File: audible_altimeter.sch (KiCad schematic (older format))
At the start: 12 parts, among them IC1 BUQ2-ATXMEGA128A4U-A, U1 MPL3115A2, U2 TAG-CONNECT-ATMEL-PDI-CONNECT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, U3 MICRO-SD-CONN, U4 MPU-9250, U5 MCP7940M, U6 MCP73831-SOT-23-5, U7 NCP4681-SC-70, U8 CSS-0575A-SMT, U9 LS013B4DN04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

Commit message: Component assignements
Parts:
- removed CON?: BUQ2-USB-MICRO-B, BUQ2-USB-MICRO-B-RIGHT-ANGLE-SM, symbol BUQ2-USB-MICRO-B
- added CON1: BUQ2-USB-MICRO-B, buq2:USB-MICRO-B-FCI, symbol BUQ2-USB-MICRO-B
- U1: footprint (none) -> buq2:8-TLGA
- U3: footprint (none) -> buq2:MICRO-SD-CONN-AMPHENOL-PUSH-PUSH
- U5: footprint (none) -> buq2:8-TDFN
- U6: footprint (none) -> buq2:SOT-23-5
- U7: footprint (none) -> buq2:SOT-353
- U8: footprint (none) -> buq2:BUZZER-CUI-5MM
- U9: footprint (none) -> buq2:FPC-CONN-10-FCI
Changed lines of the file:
@@
 F 0 "U1" H 3850 5950 60  0000 C CNN
 F 1 "MPL3115A2" H 3850 5150 60  0000 C CNN
-F 2 "" H 3850 5550 60  0001 C CNN
+F 2 "buq2:8-TLGA" H 3850 5550 60  0001 C CNN
 F 3 "" H 3850 5550 60  0000 C CNN
 	1    3850 5550
@@
 F 0 "U5" H 6300 4500 60  0000 C CNN
 F 1 "MCP7940M" H 6300 5500 60  0000 C CNN
-F 2 "" H 6350 4850 60  0001 C CNN
+F 2 "buq2:8-TDFN" H 6350 4850 60  0001 C CNN
 F 3 "" H 6350 4850 60  0000 C CNN
 	1    6350 4850
@@
 F 0 "U9" H 10100 3550 60  0000 C CNN
 F 1 "LS013B4DN04" H 10050 5500 60  0000 C CNN
-F 2 "" H 9750 4700 60  0001 C CNN
+F 2 "buq2:FPC-CONN-10-FCI" H 9750 4700 60  0001 C CNN
 F 3 "" H 9750 4700 60  0000 C CNN
 	1    9750 4700
@@
 F 0 "U8" H 9650 3000 60  0000 C CNN
 F 1 "CSS-0575A-SMT" H 9750 3950 60  0000 C CNN
-F 2 "" H 9400 3050 60  0001 C CNN
+F 2 "buq2:BUZZER-CUI-5MM" H 9400 3050 60  0001 C CNN
 F 3 "" H 9400 3050 60  0000 C CNN
 	1    9400 3050
@@
 F 0 "U6" H 8100 6200 60  0000 C CNN
 F 1 "MCP73831-SOT-23-5" H 8100 7100 60  0000 C CNN
-F 2 "" H 8100 6200 60  0001 C CNN
+F 2 "buq2:SOT-23-5" H 8100 6200 60  0001 C CNN
 F 3 "" H 8100 6200 60  0000 C CNN
 	1    8100 6200
@@
 F 0 "U3" H 5850 6300 60  0000 C CNN
 F 1 "MICRO-SD-CONN" H 5850 7850 60  0000 C CNN
-F 2 "" H 5850 6950 60  0001 C CNN
+F 2 "buq2:MICRO-SD-CONN-AMPHENOL-PUSH-PUSH" H 5850 6950 60  0001 C CNN
 F 3 "" H 5850 6950 60  0000 C CNN
 	1    5850 6950
@@
 F 0 "U7" H 8750 950 60  0000 C CNN
 F 1 "NCP4681-SC-70" H 8800 1750 60  0000 C CNN
-F 2 "" H 8750 850 60  0001 C CNN
+F 2 "buq2:SOT-353" H 8750 850 60  0001 C CNN
 F 3 "" H 8750 850 60  0000 C CNN
 	1    8750 1400
@@
 $EndComp
 $Comp
-L BUQ2-USB-MICRO-B CON?
-U 1 1 5443C89D
-P 1350 5750
-F 0 "CON?" H 1100 6200 60  0000 C CNN
-F 1 "BUQ2-USB-MICRO-B" H 1300 5250 60  0000 C CNN
-F 2 "BUQ2-USB-MICRO-B-RIGHT-ANGLE-SM" H 1400 5050 60  0001 C CNN
-F 3 "http://portal.fciconnect.com/Comergent//fci/drawing/10118193.pdf" H 1800 5150 60  0001 C CNN
-F 4 "609-4616-1-ND" H 1500 6300 60  0001 C CNN "Digikey"
-	1    1350 5750
+L BUQ2-USB-MICRO-B CON1
+U 1 1 5443CC8A
+P 1600 5350
+F 0 "CON1" H 1350 5800 60  0000 C CNN
+F 1 "BUQ2-USB-MICRO-B" H 1550 4850 60  0000 C CNN
+F 2 "buq2:USB-MICRO-B-FCI" H 1650 4650 60  0001 C CNN
+F 3 "http://portal.fciconnect.com/Comergent//fci/drawing/10118193.pdf" H 2050 4750 60  0001 C CNN
+F 4 "609-4616-1-ND" H 1750 5900 60  0001 C CNN "Digikey"
+	1    1600 5350
 	1    0    0    -1
 $EndComp

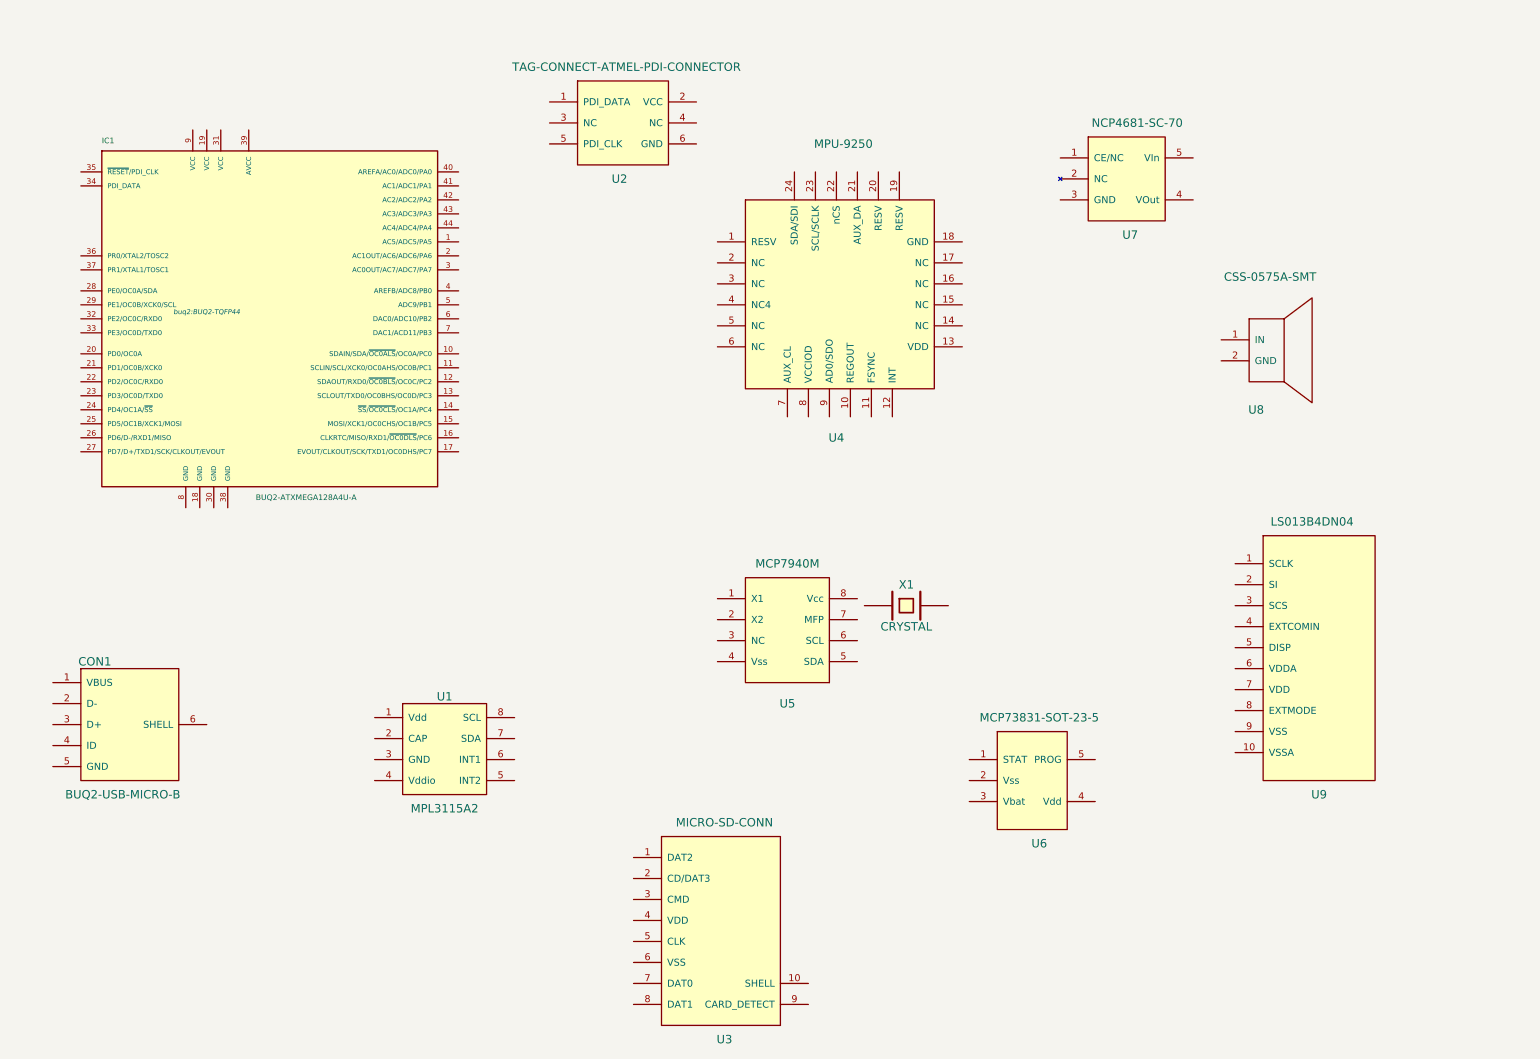
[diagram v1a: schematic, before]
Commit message: Start adding power components
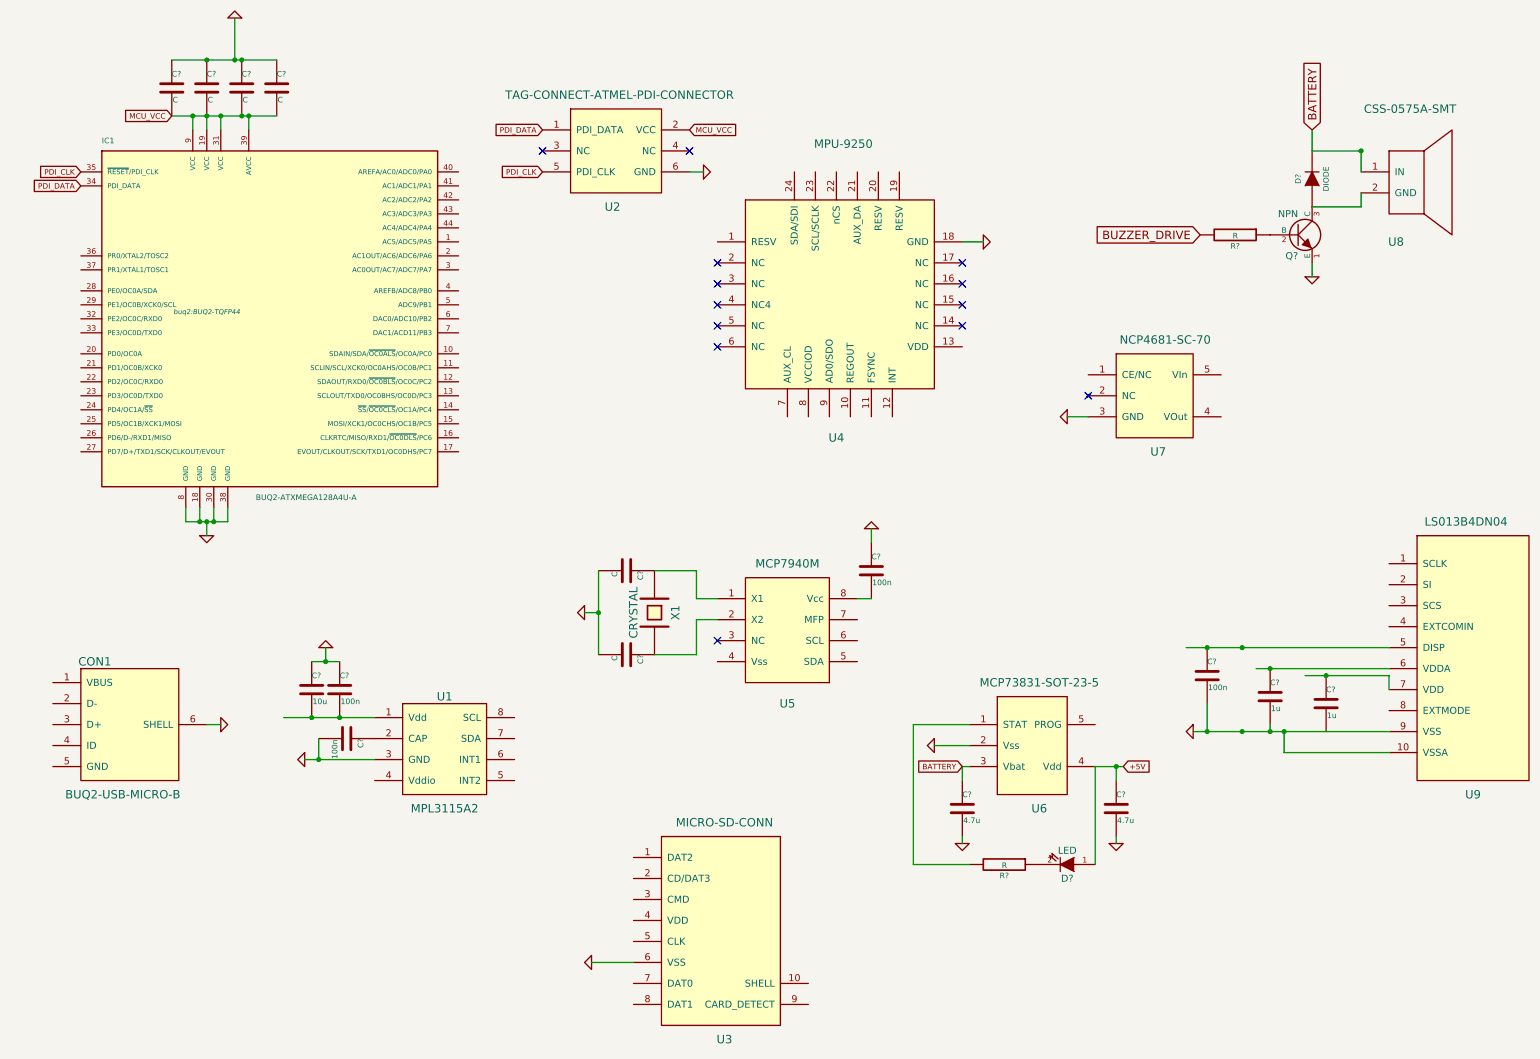
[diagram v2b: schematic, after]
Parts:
- added C? (x6): C, symbol C
- added C? (x2): 4.7u, symbol C
- added C? (x4): 100n, symbol C
- added C? (x2): 1u, symbol C
- added C?: 10u, symbol C
- added D?: DIODE, symbol DIODE
- added D?: LED, symbol LED
- added Q?: NPN, symbol NPN
- added R? (x2): R, symbol R
- U4: footprint (none) -> buq2:24QFN-3MM-3MM
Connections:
- net labels added: +5V, BATTERY, BUZZER_DRIVE, GND, MCU_VCC, PDI_CLK, PDI_DATA
- wire segments 0 -> 59
- no-connect marks 0 -> 13
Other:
- moved on the sheet: U2, U6, U7, U8, U9, X1

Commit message: Assign some components
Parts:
- C10, C13, C14, C15, C6, C7, C8, C9: renamed from C?; footprint (none) -> buq2:SM0603
- C11, C12: renamed from C?; footprint (none) -> buq2:SM0805
- D1, D2: renamed from D?; footprint (none) -> buq2:SM0603
- R1, R2: renamed from R?; footprint (none) -> buq2:SM0603
- X1: footprint (none) -> buq2:SM0805
- gave numbers to parts that had none: 6

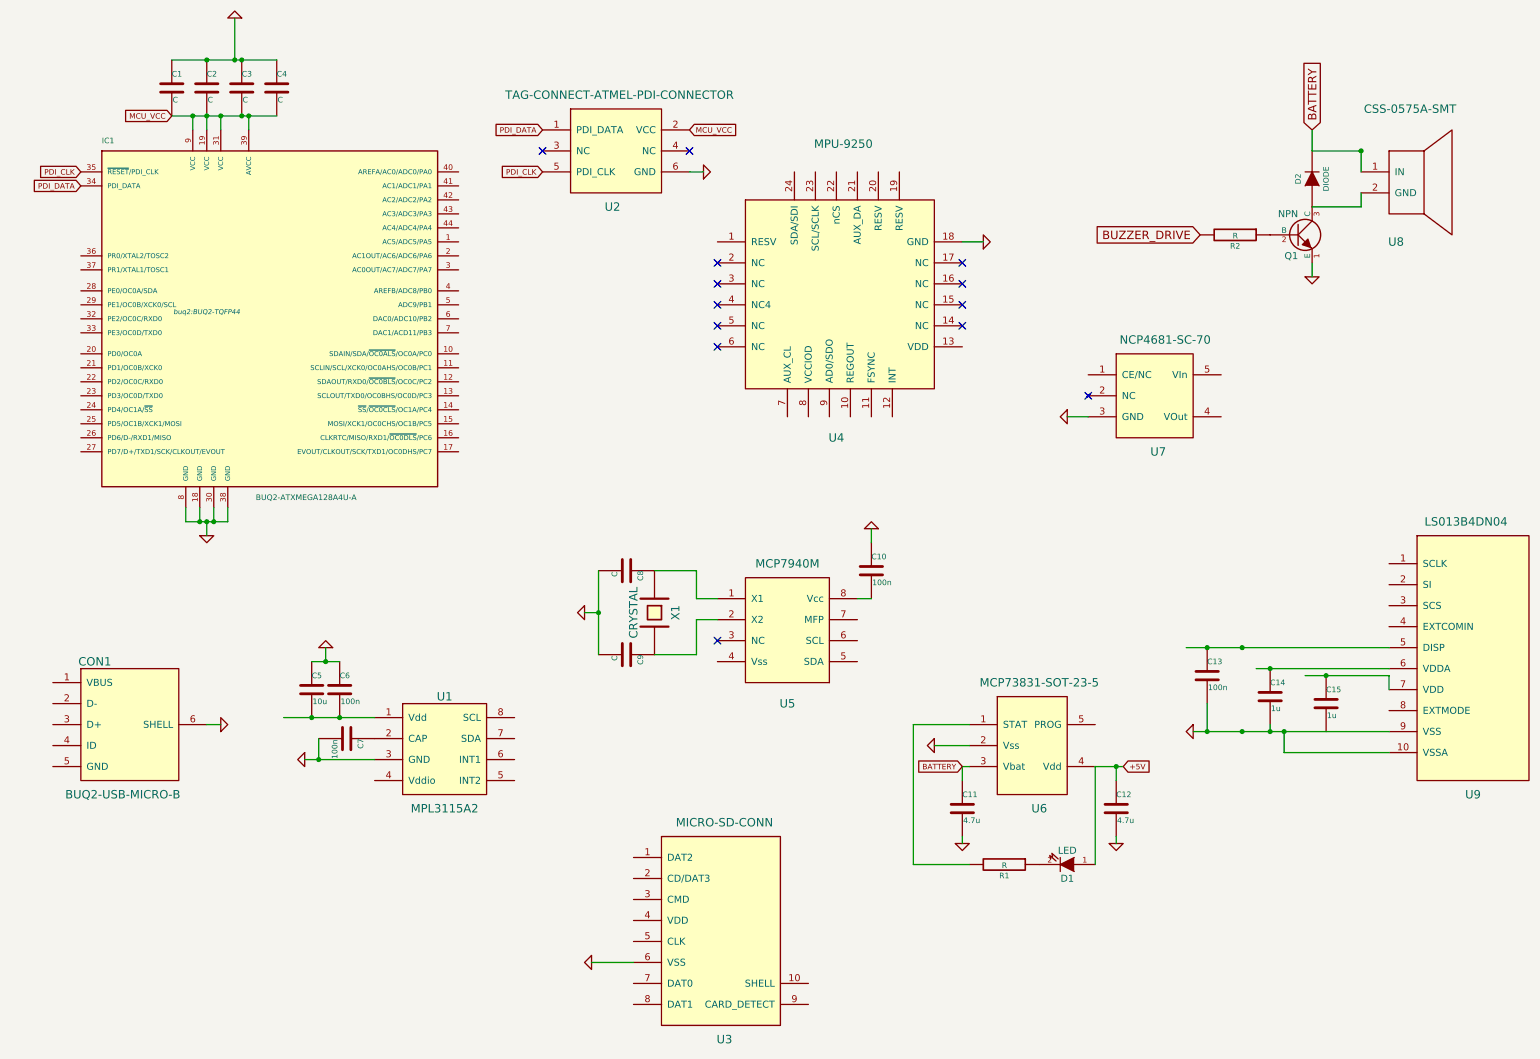
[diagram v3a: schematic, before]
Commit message: Start using hierarchical sheets
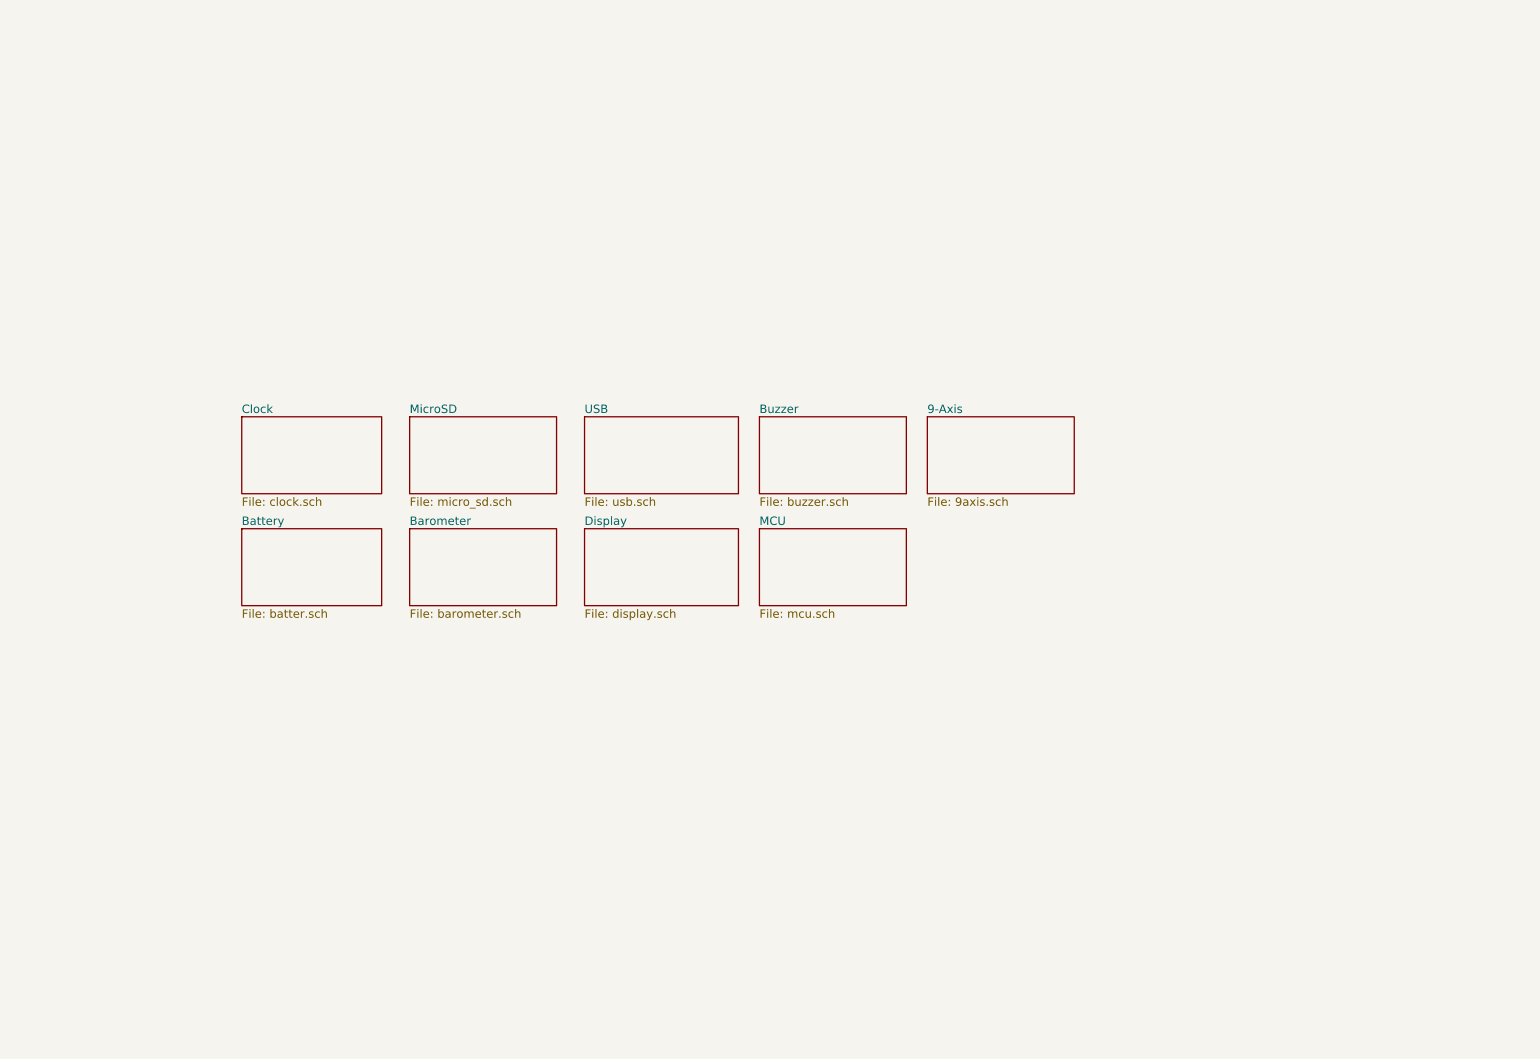
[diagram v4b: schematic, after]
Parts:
- removed C1, C2, C3, C4: C, symbol C
- removed C10, C13, C6, C7: 100n, buq2:SM0603, symbol C
- removed C11, C12: 4.7u, buq2:SM0805, symbol C
- removed C14, C15: 1u, buq2:SM0603, symbol C
- removed C5: 10u, symbol C
- removed C8, C9: C, buq2:SM0603, symbol C
- removed CON1: BUQ2-USB-MICRO-B, buq2:USB-MICRO-B-FCI, symbol BUQ2-USB-MICRO-B
- removed D1: LED, buq2:SM0603, symbol LED
- removed D2: DIODE, buq2:SM0603, symbol DIODE
- removed IC1: BUQ2-ATXMEGA128A4U-A, buq2:BUQ2-TQFP44, symbol BUQ2-ATXMEGA128A4U-A
- removed Q1: NPN, symbol NPN
- removed R1, R2: R, buq2:SM0603, symbol R
- removed U1: MPL3115A2, buq2:8-TLGA, symbol MPL3115A2
- removed U2: TAG-CONNECT-ATMEL-PDI-CONNECTOR, buq2:TAG-CONNECT6, symbol TAG-CONNECT-ATMEL-PDI-CONNECTOR
- removed U3: MICRO-SD-CONN, buq2:MICRO-SD-CONN-AMPHENOL-PUSH-PUSH, symbol MICRO-SD-CONN
- removed U4: MPU-9250, buq2:24QFN-3MM-3MM, symbol MPU-9250
- removed U5: MCP7940M, buq2:8-TDFN, symbol MCP7940M
- removed U6: MCP73831-SOT-23-5, buq2:SOT-23-5, symbol MCP73831-SOT-23-5
- removed U7: NCP4681-SC-70, buq2:SOT-353, symbol NCP4681-SC-70
- removed U8: CSS-0575A-SMT, buq2:BUZZER-CUI-5MM, symbol CSS-0575A-SMT
- removed U9: LS013B4DN04, buq2:FPC-CONN-10-FCI, symbol LS013B4DN04
- removed X1: CRYSTAL, buq2:SM0805, symbol CRYSTAL
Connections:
- net labels removed: +5V, BATTERY, BUZZER_DRIVE, GND, MCU_VCC, PDI_CLK, PDI_DATA
- wire segments 59 -> 0
- no-connect marks 13 -> 0
